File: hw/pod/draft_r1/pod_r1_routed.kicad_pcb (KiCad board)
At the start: 4 copper layers, 34 x 13 mm, 73 parts, among them J1 TestPoint_Pad_D1.0mm, J10 TestPoint_Pad_D1.0mm, J11 TestPoint_Pad_D1.0mm, J12 TestPoint_Pad_D1.0mm, J2 TestPoint_Pad_D1.0mm, J3 TestPoint_Pad_D1.0mm, J4 WirePad_1.0x2.0mm, J5 TestPoint_Pad_D1.0mm, J7 TestPoint_Pad_D1.0mm, J8 TestPoint_Pad_D1.0mm, J9 TestPoint_Pad_D1.0mm, Q1 Nexperia_SOT1216_DFN1010B-6, Q2 Nexperia_SOT1216_DFN1010B-6, SW1 SW-SMD_4P-L3.0-W2.6-P1.85-LS3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, U1 QFN-48-1EP_7x7mm_P0.5mm_EP5.6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, U2 Knowles_LGA-5_3.5x2.65mm, U3 DSBGA-8_L1.6-W0.9-R2-C4-P0.40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, U4 X2SON-4_L1.0-W1.0-P0.65-TL-EP, U6 SOT-553-5_L1.6-W1.2-P0.50-LS1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, Y1 FC-135R_L3.2-W1.5

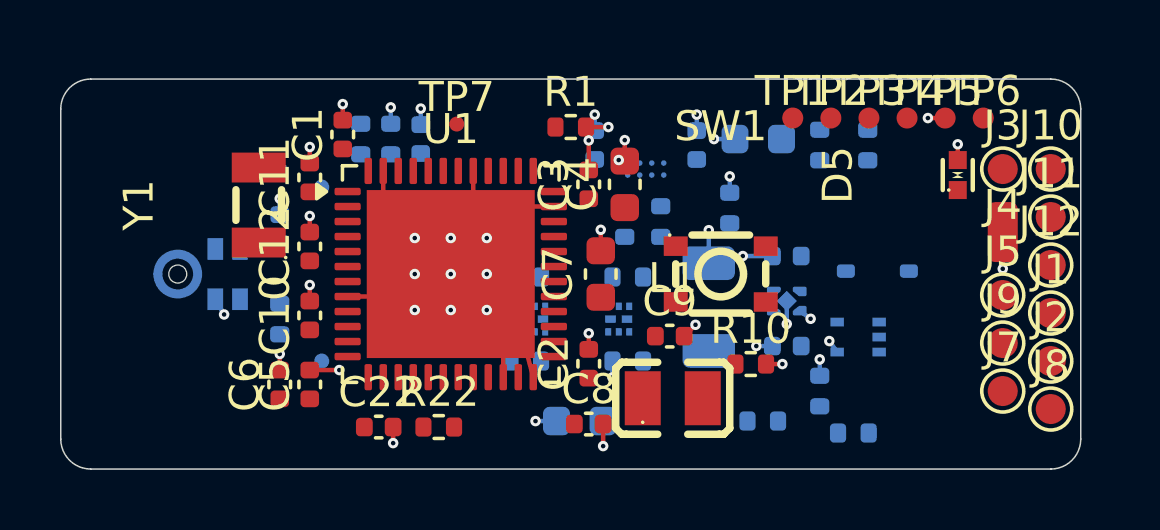
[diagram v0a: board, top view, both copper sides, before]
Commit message: Rev F routed (Phase 1 board for owner review): ECR-0003 bridge leg B -> TIM1_CH3/CH3N on PA10/PB15 (verified in ST open pin data, AF1); charger cluster shifted +2.5 mm to give the MCU's top-right pins a via field. Route: 687 tracks, 118 vias, 2 unconnected (SWCLK to TP2 ~10 mm, LED_K to J8 ~21 mm: layout-session items), DRC = pad-ring courtyards only. Tracker: R-PROC-DOCK and R-PROC-DEBUG re-modelled (no broken watches)
Co-Authored-By: Claude Opus 5.5 <noreply@anthropic.com>
Claude-Session: https://claude.ai/code/session_01Wg997D6KFs8bxoAH56jZZJ
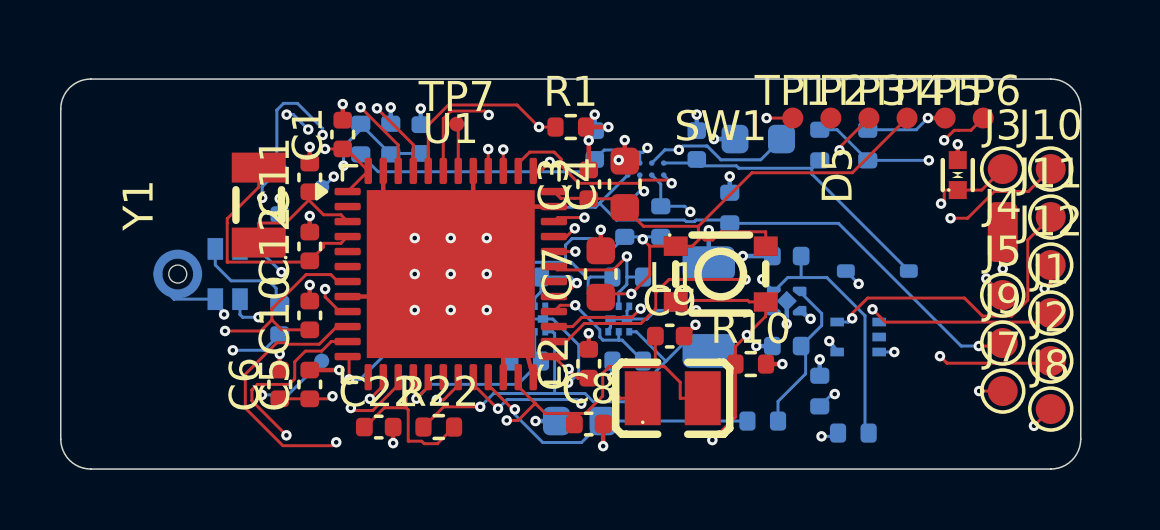
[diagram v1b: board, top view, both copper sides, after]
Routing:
- net +3V0: track 0.00 -> 76.3 mm, vias 0 -> 7
- net NRST: track 0.00 -> 45.9 mm, vias 0 -> 2
- net VBUS_SENSE: track 0.00 -> 41.4 mm, vias 0 -> 2
- net VDD11: track 0.00 -> 35.3 mm, vias 0 -> 2
- net BTN: track 0.00 -> 30.2 mm, vias 0 -> 3
- net VSYS: track 0.00 -> 29.3 mm, vias 0 -> 3
- net TS: track 0.00 -> 28.4 mm, vias 0 -> 2
- net VBAT: track 0.00 -> 27.6 mm, vias 0 -> 2
- net OUT_A: track 0.00 -> 22.8 mm, vias 0 -> 2
- net USB_DP: track 0.00 -> 22.1 mm, vias 0 -> 3
- net USB_DM: track 0.00 -> 21.2 mm, vias 0 -> 2
- net N$2: track 0.00 -> 18.9 mm, vias 0 -> 4
- net MDF_CCK: track 0.00 -> 17.8 mm, vias 0 -> 2
- net MIC_DATA: track 0.00 -> 17.0 mm, vias 0 -> 4
- net OUT_B: track 0.00 -> 16.7 mm, vias 0 -> 2
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
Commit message: Silkscreen redesign + photo renders (owner: "make sure the silkscreen looks pretty"; translucent case parts considered)
hw/pod/silk.py (post-route, idempotent, copper untouched; place_r1.py now runs it):
- reference designators -> Fab layers (52 refs cannot meet JLC's 1.0 mm legend minimum on 34x13 mm)
- footprint silk kept only for orientation-critical parts; library marks within 0.15 mm of a pad replaced by
  pin-1 dots placed clear of pads and package bodies (U1, U3, U4, U6)
- top face: mic-port keep-clear ring + sound arcs; STEREO / ULTRASOUND / REV F name block; bottom: CELL SIDE
- board rules raised to JLC legend minimums (jlcpcb.com capabilities, read 2026-10-02): text 1.0 mm, line 0.15,
  pad clearance 0.15. DRC: silk/text 0 (was ~200 warnings); courtyards 19 and dangling vias 5 unchanged
tools/render_board.py: 3D renders in a chosen mask colour with ENIG, on the dark background; KiCad library models
from a user cache (CC-BY-SA 4.0, ~/.cache/ultrasonic/kicad3d/SOURCE.md). Owner decision: mask Black or Purple.

Co-Authored-By: Claude Opus 5.5 <noreply@anthropic.com>
Claude-Session: https://claude.ai/code/session_01Wg997D6KFs8bxoAH56jZZJ
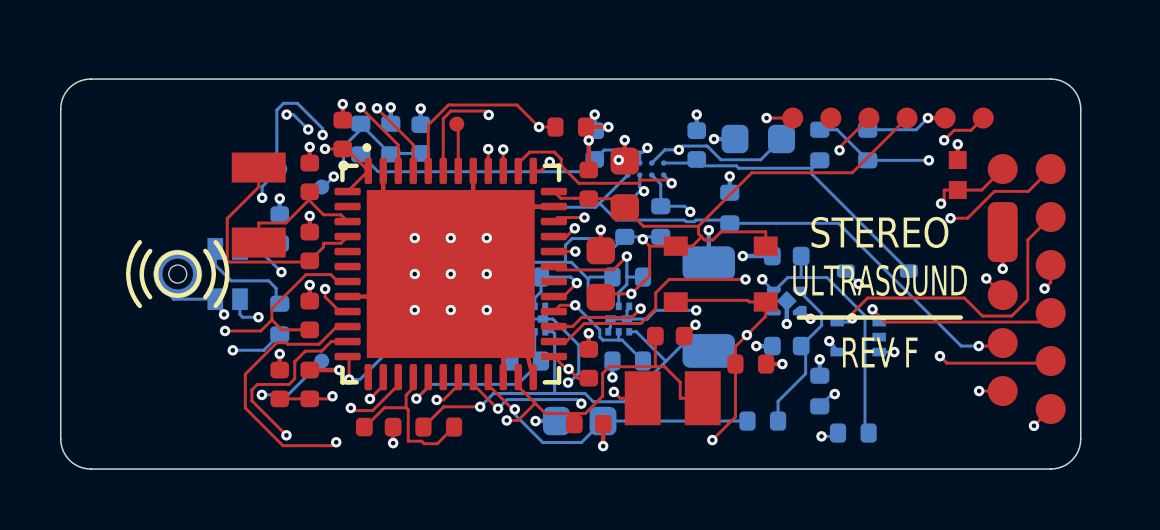
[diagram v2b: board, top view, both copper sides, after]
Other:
- board text added: "CELL SIDE"
- board text added: "REV F"
- board text added: "STEREO"
- board text added: "ULTRASOUND"

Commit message: Rev G (ECR-0017, owner O24): C8/C9 back to 10 V-rated 2.2 uF C107369 (ST DS13737 Rev 10 p.153); D6 TPD1E10B06 ESD at the exposed CC contact J12 (same part/BOM line as D5)
- gen.py Rev G: 53 placed parts, 30 BOM lines, ERC 0; bom_check identity + part_heights for C107369
- board re-placed + routed (D6 on B behind J12, one via): 694 tracks, 118 vias, 1 unconnected (I2C_SDA, router
  variance), DRC 19 courtyard + 1 clearance 0.0892 vs 0.09 mm (router rounding); Phase-2 board supersedes it
- schematic pages regenerated (D6 on the dock sheet, Rev G title): connectivity PASS, 195 memberships
- tracker: new relations R-SMPS-BOARD, R-CLOCK-BOARD, R-UI-BOARD (miniaturization MZG-15 blind spot); all reviewed,
  0 suspect / 0 stale; docs updated (sub-processing issue 1 closed, sub-dock-usb F15, reg-board route, 00-whole counts)
- interfaces.py self-test: the clamp-band victim skips test pads (exempt by rule; the re-placement put TP7 first)

Co-Authored-By: Claude Opus 5.5 <noreply@anthropic.com>
Claude-Session: https://claude.ai/code/session_01Wg997D6KFs8bxoAH56jZZJ
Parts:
- added D6: X1SON-2_L1.0-W0.6-P0.65-BI-1, X1SON-2_L1.0-W0.6-P0.65-BI-1, B.Cu at (32.6, 6.20)
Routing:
- net LED_K: track 4.21 -> 29.8 mm
- net SWCLK: track 0.67 -> 20.1 mm, vias 1 -> 4
- net NRST: track 45.9 -> 28.9 mm
- net VBUS_SENSE: track 41.4 -> 27.0 mm
- net TS: track 28.4 -> 40.1 mm, vias 2 -> 4
- net I2C_SDA: track 12.6 -> 1.25 mm, vias 2 -> 0
- net BTN: track 30.2 -> 23.2 mm, vias 3 -> 2
- net +3V0: track 76.3 -> 71.1 mm, vias 7 -> 9
- net MDF_CCK: track 17.8 -> 13.0 mm
- net SWDIO: track 14.9 -> 10.2 mm
- net CC: track 10.1 -> 14.4 mm, vias 2 -> 1
- net I2C_SCL: track 12.9 -> 8.77 mm, vias 2 -> 1
- net VSYS: track 29.3 -> 26.1 mm, vias 3 -> 5
- net OUT_A: track 22.8 -> 25.9 mm
- net USB_DP: track 22.1 -> 25.2 mm
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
